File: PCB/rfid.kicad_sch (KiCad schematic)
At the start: 38 parts, among them J5 CS01, J6 CSI1, U4 ST25R3916-AQWT, Y1 ABM8-27.120MHZ

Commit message: Schematic is almost ready
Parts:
- removed U4: ST25R3916-AQWT, External:QFN50P500X500X100-33N, symbol ST25R3916-AQWT:ST25R3916-AQWT
- added U5: ST25R3916-AQWT, External:QFN50P500X500X100-33N, symbol External:ST25R3916-AQWT
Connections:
- net +3V3: now also U5.1 (VDD_IO), U5.10 (VDD_TX)
- net AN1: now also U5.13 (RFO1)
- net AN2: now also U5.15 (RFO2)
- net DC1: now also U5.8 (VDD)
- net DC3: now also U5.14 (VDD_DR), U5.9 (VDD_RF)
- net DC4: now also U5.11 (VDD_AM)
- net DC5: now also U5.7 (VDD_A)
- net DC6: now also U5.3 (VDD_D)
- net DC7: now also U5.24 (AGDC)
- net GND: now also U5.12 (GND_DR), U5.16 (GND_DR), U5.20 (I2C_EN), U5.21 (VSS), U5.26 (GND_A), U5.33 (EXP), U5.6 (GND_D)
- net NFC_IRQ: now also U5.27 (IRQ)
- net NFC_MISO: now also U5.32 (MISO/SDA)
- net NFC_MOSI: now also U5.31 (MOSI)
- net NFC_NSS: now also U5.29 (~{BSS})
- net NFC_SCK: now also U5.30 (SCLK/SCL)
- net at C9.2, Y1.1: now also U5.5 (XTI)
- net at J5.1 (Pin_1): now also U5.2 (CSO)
- net at C15.1: now also U5.23 (RFI2)
- net at C14.1: now also U5.22 (RFI1)
- net at J6.1 (Pin_1): now also U5.25 (CSI)
- net at C10.1, Y1.3: now also U5.4 (XTO)

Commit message: PN532 pins are added
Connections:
- net +3V3 renamed BAT+
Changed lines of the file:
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@@
 		(in_pos_files yes)
 		(dnp no)
-		(fields_autoplaced yes)
 		(property "Reference" "#PWR050"
 			(at 147.32 63.5 0)
@@
 			)
 		)
-		(property "Value" "+3V3"
-			(at 147.32 54.61 0)
+		(property "Value" "BAT+"
+			(at 148.336 56.896 0)
 			(show_name no)
 			(do_not_autoplace no)
@@
 					(size 1.27 1.27)
 				)
+				(justify left)
 			)
 		)

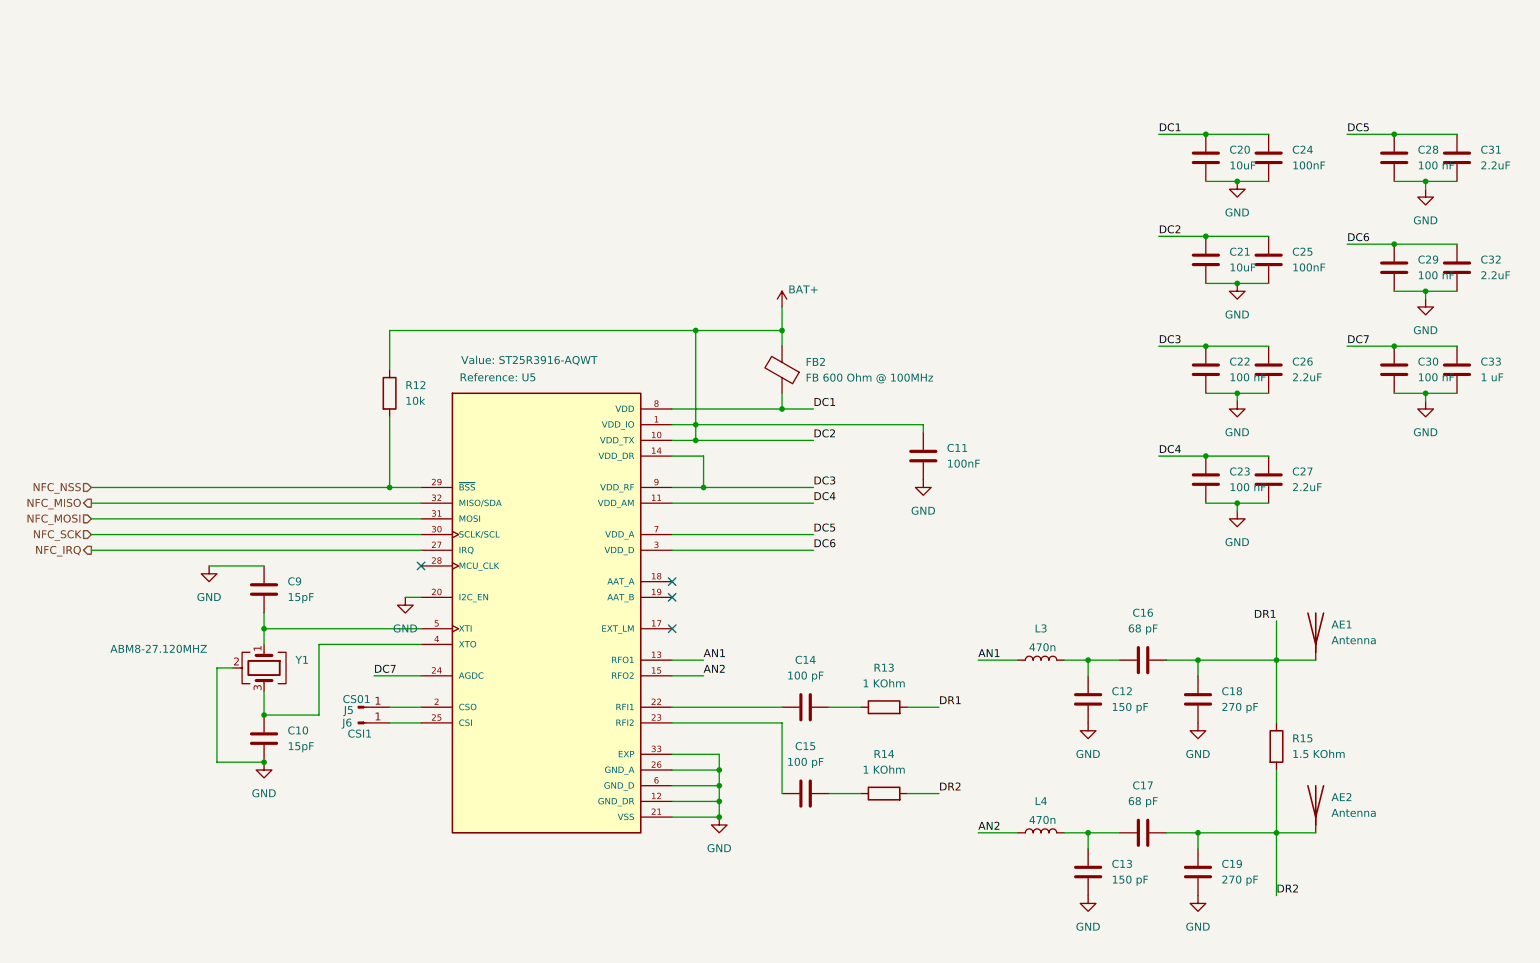
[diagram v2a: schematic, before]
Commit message: ESD diodes added
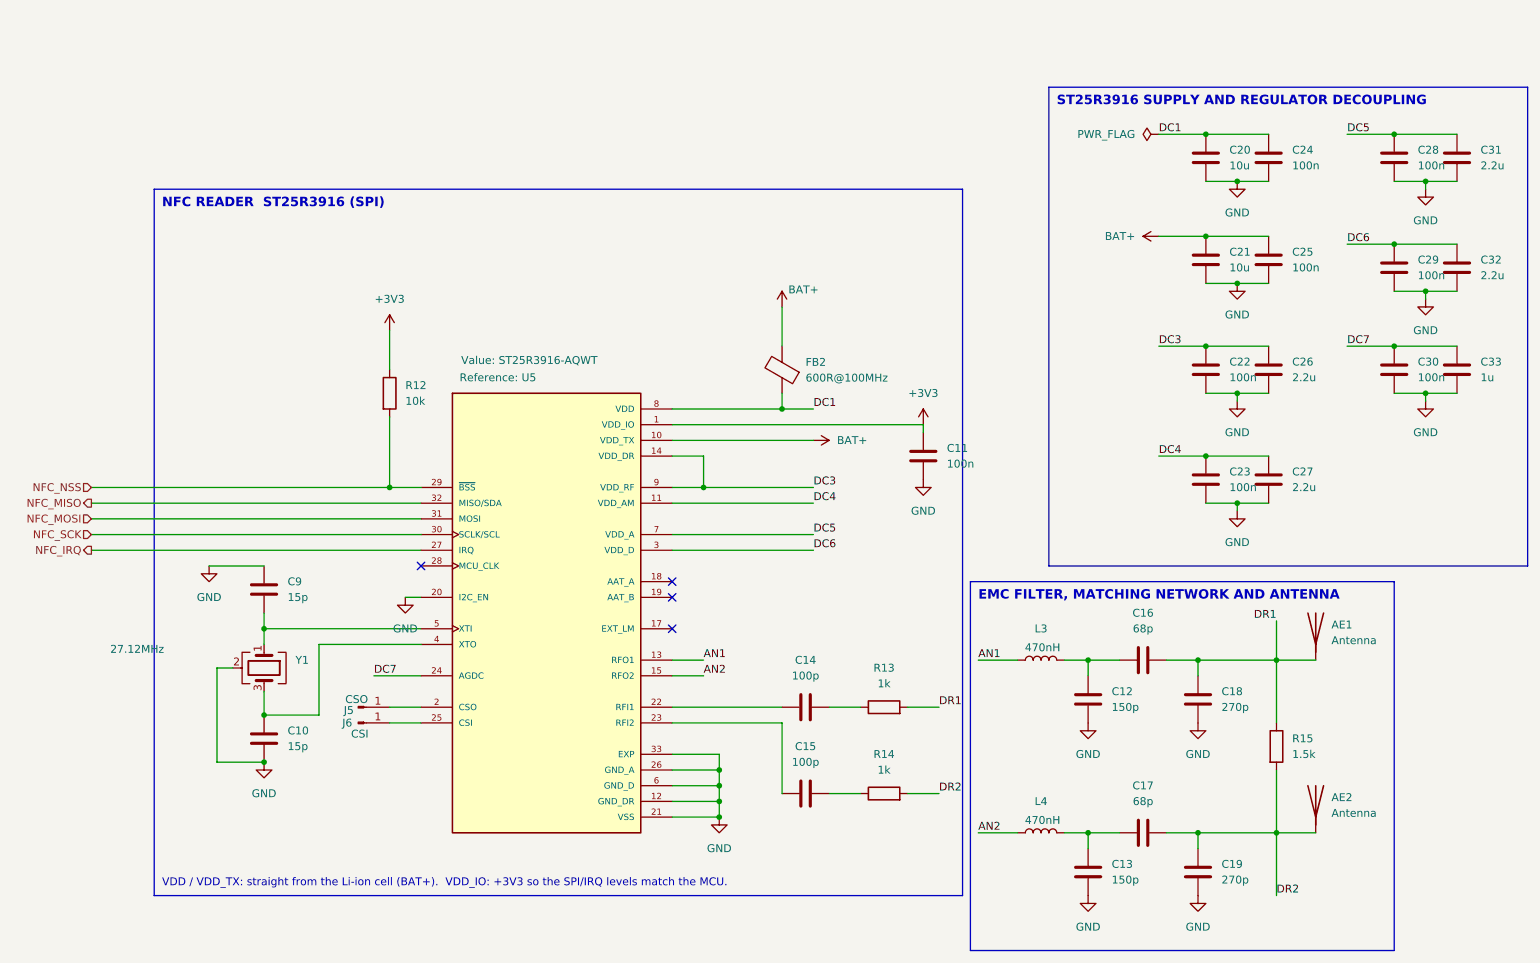
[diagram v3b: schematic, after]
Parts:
- C10, C9: value 15pF -> 15p; Dielectric (none) -> C0G; Voltage (none) -> 50V
- C11, C24, C25: value 100nF -> 100n; Dielectric (none) -> X7R; Voltage (none) -> 16V
- C12, C13: value 150 pF -> 150p; Dielectric (none) -> C0G; Voltage (none) -> 50V
- C14, C15: value 100 pF -> 100p; Dielectric (none) -> C0G; Voltage (none) -> 50V
- C16, C17: value 68 pF -> 68p; Dielectric (none) -> C0G; Voltage (none) -> 50V
- C18, C19: value 270 pF -> 270p; Dielectric (none) -> C0G; Voltage (none) -> 50V
- C20, C21: value 10uF -> 10u; Dielectric (none) -> X5R; Voltage (none) -> 10V
- C22, C23, C28, C29, C30: value 100 nF -> 100n; Dielectric (none) -> X7R; Voltage (none) -> 16V
- C26, C27, C31, C32: value 2.2uF -> 2.2u; Dielectric (none) -> X5R; Voltage (none) -> 10V
- C33: value 1 uF -> 1u; Dielectric (none) -> X5R; Voltage (none) -> 10V
- FB2: value FB 600 Ohm @ 100MHz -> 600R@100MHz
- J5: value CS01 -> CSO
- J6: value CSI1 -> CSI
- L3, L4: value 470n -> 470nH
- R13, R14: value 1 KOhm -> 1k
- R15: value 1.5 KOhm -> 1.5k
- Y1: value ABM8-27.120MHZ -> 27.12MHz; MPN (none) -> ABM8-27.120MHZ
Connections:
- net BAT+: no longer C11.1, R12.1, U5.1 (VDD_IO)
- new net +3V3: C11.1, R12.1, U5.1 (VDD_IO)
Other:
- note added: "EMC FILTER, MATCHING NETWORK AND ANTENNA"
- note added: "NFC READER ST25R3916 (SPI)"
- note added: "ST25R3916 SUPPLY AND REGULATOR DECOUPLING"
- note added: "VDD / VDD_TX: straight from the Li-ion cell (BAT+). VDD_IO: +3V3 so the SPI/IRQ levels match the MCU."
- title: (none) -> Card Attendance System

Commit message: routing complete
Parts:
- removed AE1, AE2: Antenna, symbol Device:Antenna
- removed C14: 100p, Capacitor_SMD:C_0805_2012Metric, symbol Device:C
- removed R13, R14: 1k, Resistor_SMD:R_0805_2012Metric, symbol Device:R
- added AE3: Antenna_Loop, NetTie:NetTie-2_SMD_Pad0.5mm, symbol Device:Antenna_Loop
- added C37: 10p, Capacitor_SMD:C_0805_2012Metric, symbol Device:C
- added C38, C39: 150p, Capacitor_SMD:C_0805_2012Metric, symbol Device:C
- added R21, R22: 0, Resistor_SMD:R_0805_2012Metric, symbol Device:R
- C15: value 100p -> 10p
- L3, L4: footprint Inductor_SMD:L_0402_1005Metric -> Inductor_SMD:L_0805_2012Metric_Pad1.05x1.20mm_HandSolder
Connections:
- net DR1: now also C37.1, R21.1
- net DR2: now also C15.2, R22.2
- net GND: now also C38.1, C39.2
- net at C15.1, U5.23 (RFI2): now also C39.1
- net at U5.22 (RFI1): now also C37.2, C38.2
- new net: AE3.1, R21.2
- new net: AE3.2, R22.1
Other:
- moved on the sheet: C15

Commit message: BOMs updated
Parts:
- AE3: footprint NetTie:NetTie-2_SMD_Pad0.5mm -> Snapeda:NFC_Loop_40x30_3T
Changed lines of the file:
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@@
 			)
 		)
-		(property "Footprint" "NetTie:NetTie-2_SMD_Pad0.5mm"
+		(property "Footprint" "Snapeda:NFC_Loop_40x30_3T"
 			(at 241.3 129.54 0)
 			(hide yes)

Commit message: almost ready for fabrication
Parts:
- C12: renamed from C9; LCSC (none) -> C107110
- C13: renamed from C10; LCSC (none) -> C107110
- C14: renamed from C38; LCSC (none) -> C107111
- C15: renamed from C39; LCSC (none) -> C107111
- C16: renamed from C37; LCSC (none) -> C107107
- C17: renamed from C15; LCSC (none) -> C107107
- C18: renamed from C11; LCSC (none) -> C49678
- C19: renamed from C12; LCSC (none) -> C107111
- C20: renamed from C13; LCSC (none) -> C107111
- C21: renamed from C16; LCSC (none) -> C107120
- C22: renamed from C17; LCSC (none) -> C107120
- C23: renamed from C18; LCSC (none) -> C107106
- C24: renamed from C19; LCSC (none) -> C107106
- C25: renamed from C20; LCSC (none) -> C15850
- C26: renamed from C21; LCSC (none) -> C15850
- C27: renamed from C22; LCSC (none) -> C49678
- C28: renamed from C23; LCSC (none) -> C49678
- C29: renamed from C24; LCSC (none) -> C49678
- C30: renamed from C25; LCSC (none) -> C49678
- C31: renamed from C26; LCSC (none) -> C377773
- C32: renamed from C27; LCSC (none) -> C377773
- C33: renamed from C28; LCSC (none) -> C49678
- C34: renamed from C29; LCSC (none) -> C49678
- C35: renamed from C30; LCSC (none) -> C49678
- C36: renamed from C31; LCSC (none) -> C377773
- C37: renamed from C32; LCSC (none) -> C377773
- C38: renamed from C33; LCSC (none) -> C28323
- FB2: LCSC (none) -> C76884
- L1: renamed from L3; LCSC (none) -> C337959
- L2: renamed from L4; LCSC (none) -> C337959
- R17: renamed from R12; LCSC (none) -> C17414
- R18: renamed from R15; LCSC (none) -> C4310
- R19: renamed from R21; LCSC (none) -> C17477
- R20: renamed from R22; LCSC (none) -> C17477
- U5: LCSC (none) -> C2908147
- Y2: renamed from Y1; LCSC (none) -> C29975; MPN ABM8-27.120MHZ -> X32252712MMB4SI
- renumbered AE3 to AE1, J5 to J6, J6 to J7

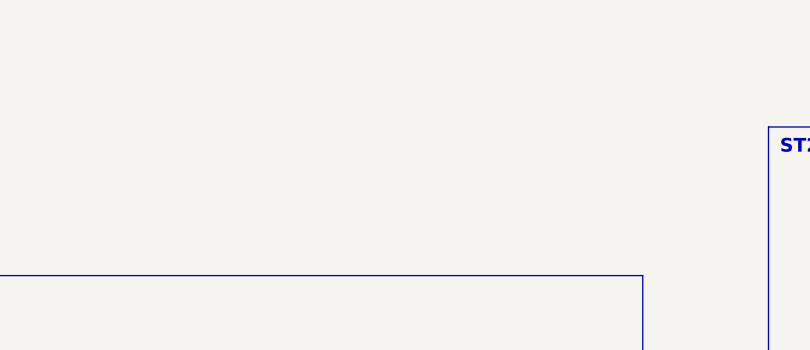
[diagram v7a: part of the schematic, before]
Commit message: Mounting holes and WX logo added
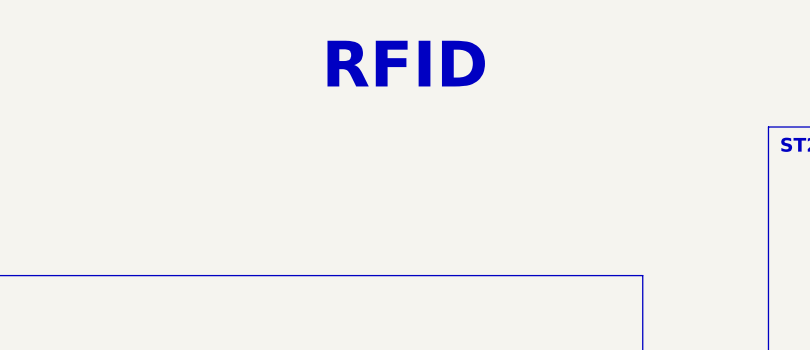
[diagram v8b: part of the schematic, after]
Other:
- note added: "RFID"
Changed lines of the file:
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@@
+		)
+	)
+	(text "RFID"
+		(exclude_from_sim no)
+		(at 150.114 17.526 0)
+		(effects
+			(font
+				(size 5.08 5.08)
+				(thickness 1.524)
+				(bold yes)
+			)
 		)
 	)
